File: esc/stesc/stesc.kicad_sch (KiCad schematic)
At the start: 2 parts, among them J3 5530843-7, U3 B-G431B-ESC1

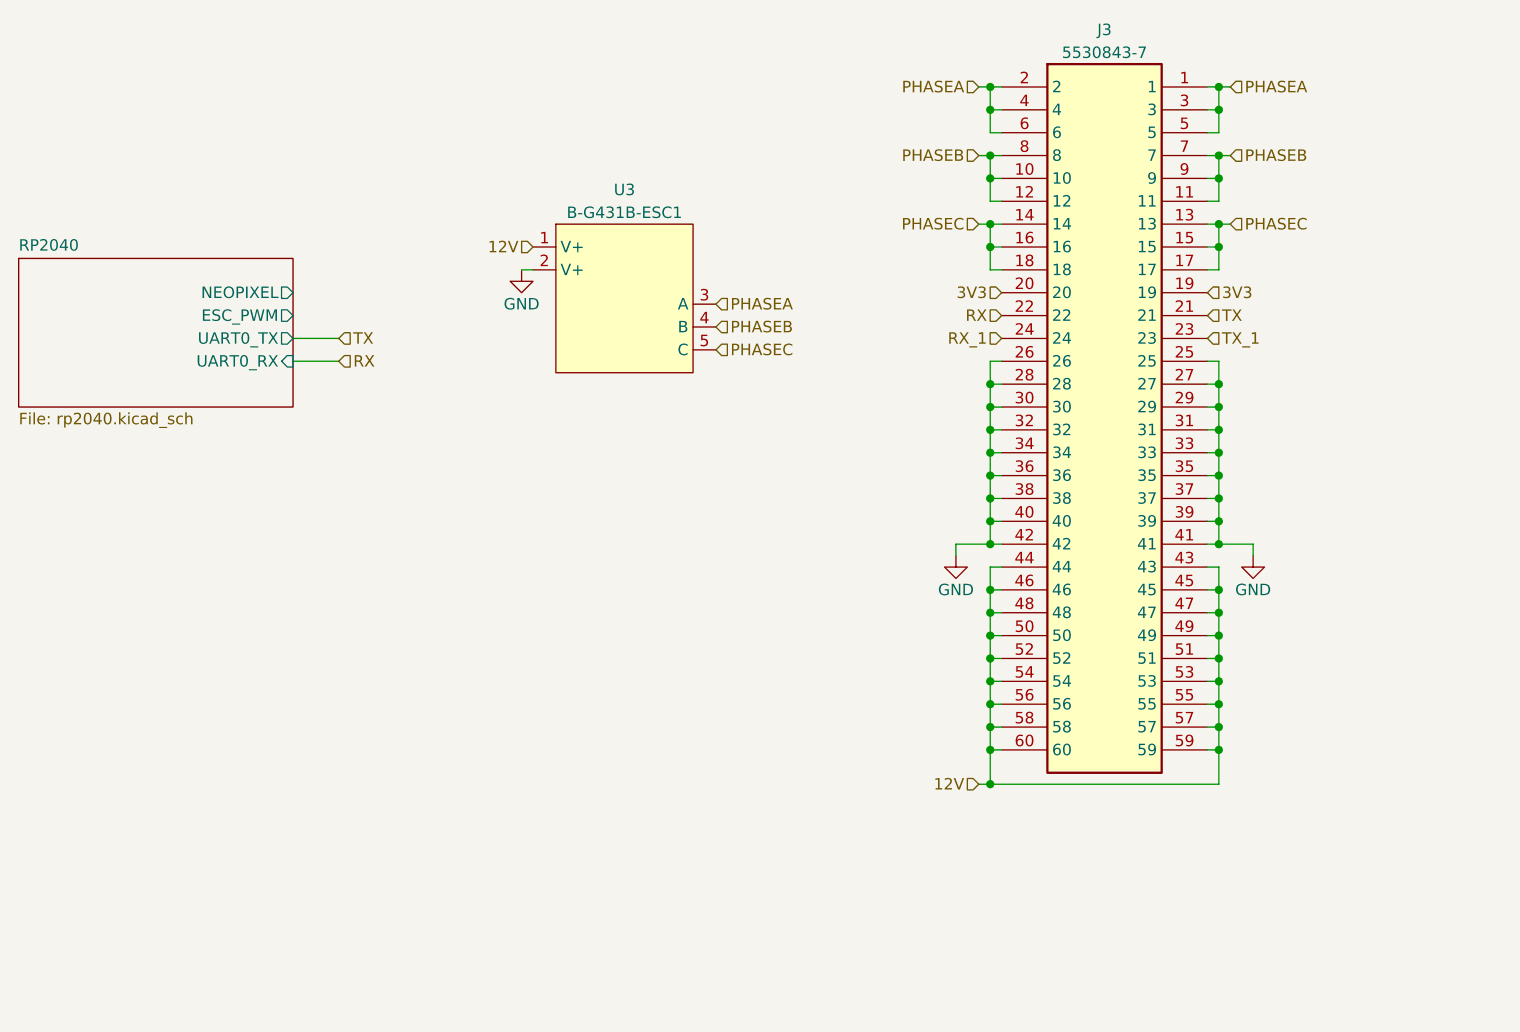
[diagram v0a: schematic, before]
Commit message: Feat[stesc]: refactored project and finished draft
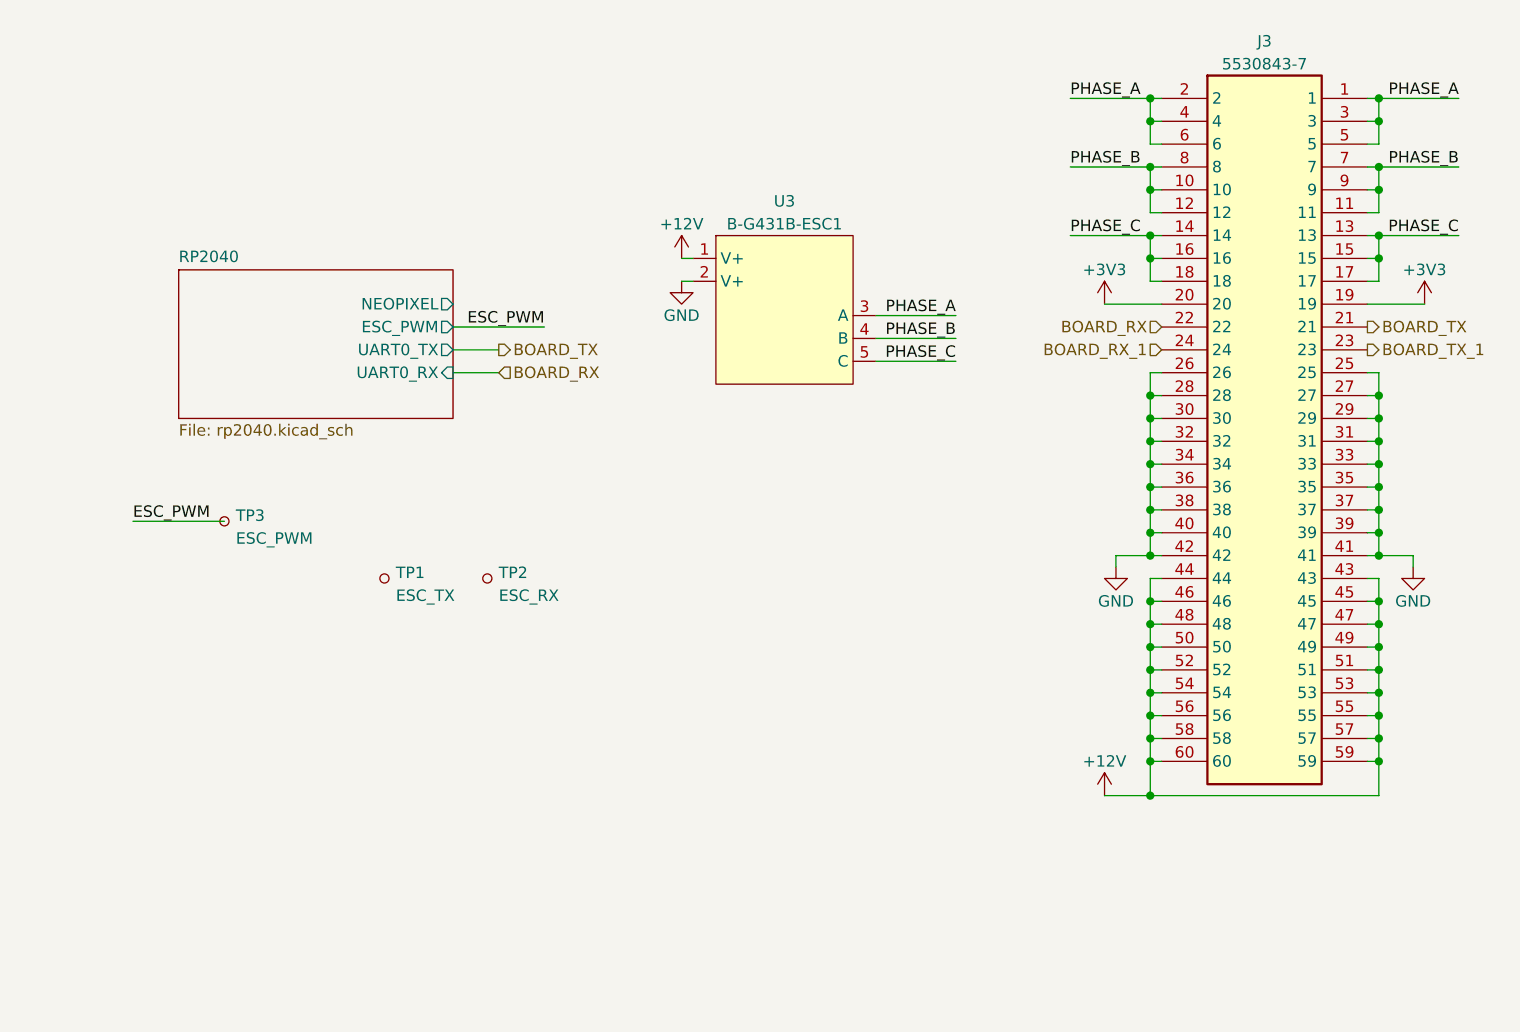
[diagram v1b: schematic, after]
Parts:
- added TP1: ESC_TX, TestPoint:TestPoint_THTPad_D2.5mm_Drill1.2mm, symbol Connector:TestPoint_Small
- added TP2: ESC_RX, TestPoint:TestPoint_THTPad_D2.5mm_Drill1.2mm, symbol Connector:TestPoint_Small
- added TP3: ESC_PWM, TestPoint:TestPoint_THTPad_D2.5mm_Drill1.2mm, symbol Connector:TestPoint_Small
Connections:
- net 12V renamed +12V
- net 3V3 renamed +3V3
- net PHASEA renamed PHASE_A
- net PHASEB renamed PHASE_B
- net PHASEC renamed PHASE_C
- net RX renamed BOARD_RX
- net RX_1 renamed BOARD_RX_1
- net TX renamed BOARD_TX
- net TX_1 renamed BOARD_TX_1
- new net ESC_PWM: TP3.1
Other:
- moved on the sheet: J3, U3

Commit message: Feat[stesc]: v1.0 draft complete
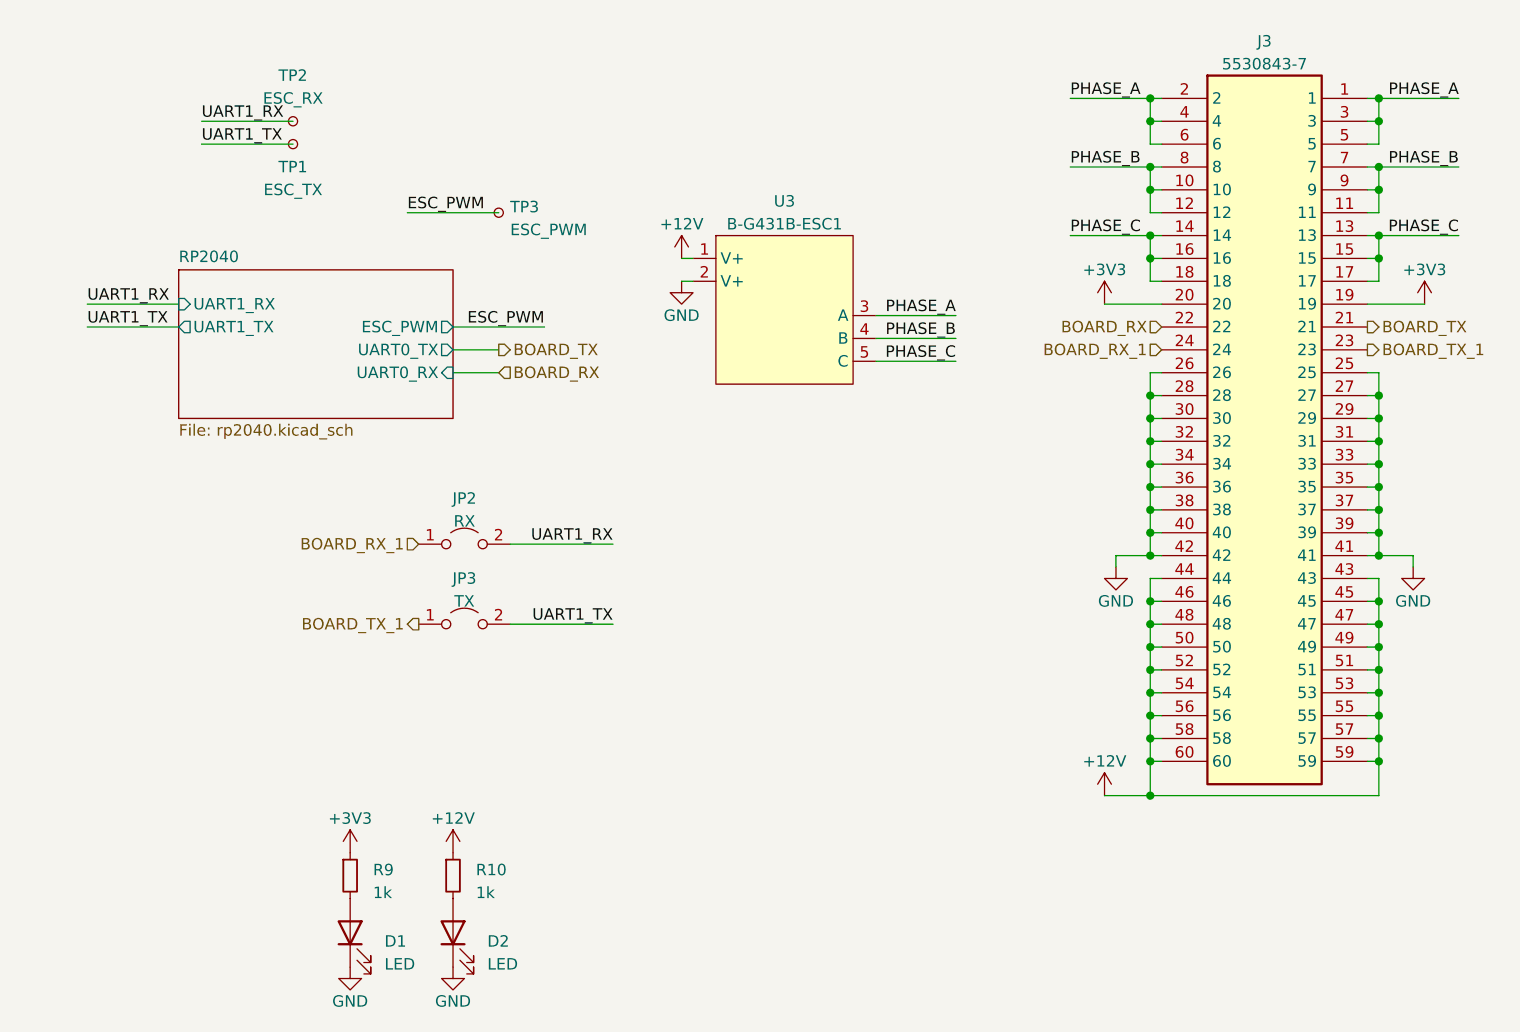
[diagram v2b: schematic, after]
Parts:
- added D1, D2: LED, LED_SMD:LED_0603_1608Metric, symbol Device:LED
- added JP2: RX, Jumper:SolderJumper-2_P1.3mm_Open_RoundedPad1.0x1.5mm, symbol Jumper:Jumper_2_Open
- added JP3: TX, Jumper:SolderJumper-2_P1.3mm_Open_RoundedPad1.0x1.5mm, symbol Jumper:Jumper_2_Open
- added R10, R9: 1k, Resistor_SMD:R_0402_1005Metric, symbol Device:R_Small
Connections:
- net +12V: now also R10.1
- net +3V3: now also R9.1
- net BOARD_RX_1: now also JP2.1 (A)
- net BOARD_TX_1: now also JP3.1 (A)
- net GND: now also D1.1 (K), D2.1 (K)
- net UART1_RX: now reaches TP2.1
- net UART1_RX: now also JP2.2 (B)
- net UART1_TX: now reaches TP1.1
- net UART1_TX: now also JP3.2 (B)
- new net: D1.2 (A), R9.2
- new net: D2.2 (A), R10.2
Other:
- sheet RP2040 ports: added UART1_RX, UART1_TX; removed NEOPIXEL
- moved on the sheet: TP1, TP2, TP3
